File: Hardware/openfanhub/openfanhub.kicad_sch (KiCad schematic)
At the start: 56 parts, among them J1 UART, J2 I2C, J3 Power input, J4 SWD, U1 STM32F103C8T8_Board, U2 AMS1117, U3 USB_HEADER_IN, U4 USB_HEADER_OUT, U5 STM32F103C8Tx, U6 AMS1117, Y1 Crystal

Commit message: Add first (badly) routed version. Still need to polish it and check all power/signal paths
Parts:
- removed J3: Power input, Connector_PinHeader_2.54mm:PinHeader_1x04_P2.54mm_Vertical, symbol Connector:Conn_01x04_Female
- added H1, H2, H3, H4: MountingHole, MountingHole:MountingHole_3.2mm_M3, symbol Mechanical:MountingHole
- added J3: 12V in, Connector_Wire:SolderWire-2.5sqmm_1x01_D2.4mm_OD4.4mm, symbol Connector:Conn_01x01_Male
- added J4: GND in, Connector_Wire:SolderWire-2.5sqmm_1x01_D2.4mm_OD4.4mm, symbol Connector:Conn_01x01_Male
- added J5: 5V IN, Connector_Wire:SolderWire-2.5sqmm_1x01_D2.4mm_OD4.4mm, symbol Connector:Conn_01x01_Male
- renumbered C5 to C1, C13 to C10, C14 to C11, C15 to C12, C16 to C13, C1 to C14, C17 to C15, C2 to C16, C18 to C17, C3 to C18, C4 to C19, C6 to C2, C7 to C3, C8 to C4, C9 to C5, C10 to C6, C11 to C7, C19 to C8, C12 to C9, FB2 to FB1, J4 to J6, R27 to R1, R26 to R10, R2 to R11, R32 to R12, R33 to R13, R3 to R14, R6 to R15, R28 to R2, R4 to R3, R29 to R4, R30 to R5, R5 to R6, R1 to R7, R31 to R8, R25 to R9, U5 to U2, U2 to U3, U6 to U4, U3 to U5, U4 to U6
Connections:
- net +12V: now also J3.1 (Pin_1)
- net +5V: now also J5.1 (Pin_1)
- net FAN1_PWM: now also U1.36 (B8), U2.45 (PB8); no longer U1.26 (A9), U2.30 (PA9)
- net FAN5_PWM: now also U1.26 (A9), U2.30 (PA9); no longer U1.36 (B8), U2.45 (PB8)
- net GND: now also J4.1 (Pin_1)

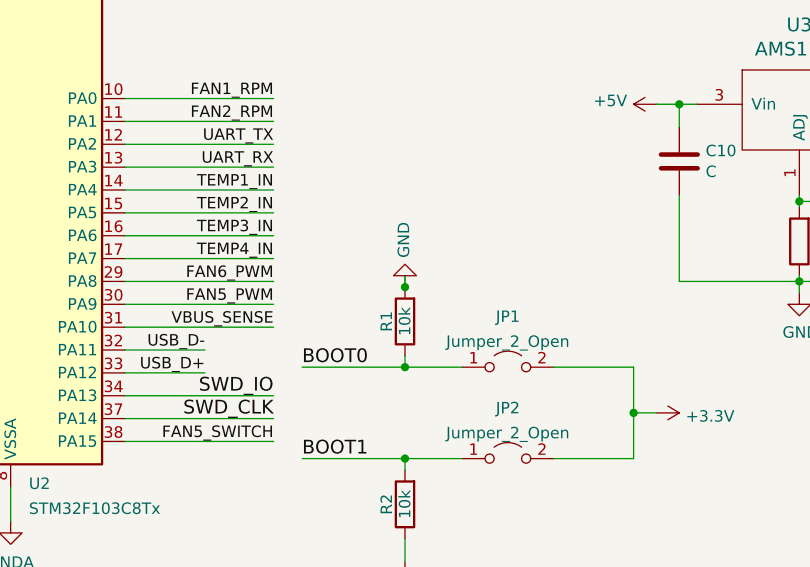
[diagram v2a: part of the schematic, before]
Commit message: Update PCB. Move Power and USB to the same side
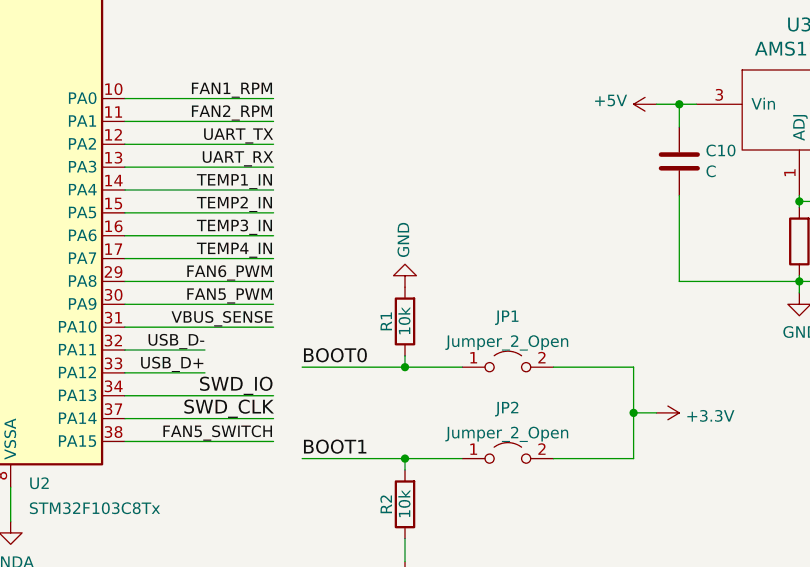
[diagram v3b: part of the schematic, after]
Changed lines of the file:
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@@
   (junction (at 123.19 42.545) (diameter 0) (color 0 0 0 0)
   )
-  (junction (at 116.205 156.21) (diameter 0) (color 0 0 0 0)
-  )
   (junction (at 221.615 136.525) (diameter 0) (color 0 0 0 0)
   )
@@
     (stroke (width 0) (type default) (color 0 0 0 0))
   )
-  (wire (pts (xy 116.205 156.21) (xy 116.205 154.94))
-    (stroke (width 0) (type default) (color 0 0 0 0))
-  )
   (wire (pts (xy 184.785 45.72) (xy 210.185 45.72))
     (stroke (width 0) (type default) (color 0 0 0 0))
@@
     )
     (path "/00000000-0000-0000-0000-000061cbd2d4/400d7499-cda1-432f-a720-e9564b76ff05/00000000-0000-0000-0000-000061cfaf6a"
-      (reference "Q1") (unit 1) (value "Q_NMOS_GSD") (footprint "Package_TO_SOT_SMD:SOT-23")
+      (reference "Q1") (unit 1) (value "IRLML2502") (footprint "Package_TO_SOT_SMD:SOT-23")
     )
     (path "/00000000-0000-0000-0000-000061cbd2d4/400d7499-cda1-432f-a720-e9564b76ff05/832da771-3447-4aa3-a1d5-34305654223f"
-      (reference "Q2") (unit 1) (value "AO449") (footprint "Package_SO:SOIC-8_3.9x4.9mm_P1.27mm")
+      (reference "Q2") (unit 1) (value "AO4409") (footprint "Package_SO:SOIC-8_3.9x4.9mm_P1.27mm")
     )
     (path "/00000000-0000-0000-0000-000061cbd2d4/374ddff5-0da3-4c1a-9cf4-3e7dd0779e2b/00000000-0000-0000-0000-000061cfaf6a"
-      (reference "Q3") (unit 1) (value "Q_NMOS_GSD") (footprint "Package_TO_SOT_SMD:SOT-23")
+      (reference "Q3") (unit 1) (value "IRLML2502") (footprint "Package_TO_SOT_SMD:SOT-23")
     )
     (path "/00000000-0000-0000-0000-000061cbd2d4/374ddff5-0da3-4c1a-9cf4-3e7dd0779e2b/832da771-3447-4aa3-a1d5-34305654223f"
-      (reference "Q4") (unit 1) (value "AO449") (footprint "Package_SO:SOIC-8_3.9x4.9mm_P1.27mm")
+      (reference "Q4") (unit 1) (value "AO4409") (footprint "Package_SO:SOIC-8_3.9x4.9mm_P1.27mm")
     )
     (path "/00000000-0000-0000-0000-000061cbd2d4/00000000-0000-0000-0000-000061cbf096/00000000-0000-0000-0000-000061cfaf6a"
-      (reference "Q5") (unit 1) (value "Q_NMOS_GSD") (footprint "Package_TO_SOT_SMD:SOT-23")
+      (reference "Q5") (unit 1) (value "IRLML2502") (footprint "Package_TO_SOT_SMD:SOT-23")
     )
     (path "/00000000-0000-0000-0000-000061cbd2d4/00000000-0000-0000-0000-000061cbf096/832da771-3447-4aa3-a1d5-34305654223f"
-      (reference "Q6") (unit 1) (value "AO449") (footprint "Package_SO:SOIC-8_3.9x4.9mm_P1.27mm")
+      (reference "Q6") (unit 1) (value "AO4409") (footprint "Package_SO:SOIC-8_3.9x4.9mm_P1.27mm")
     )
     (path "/00000000-0000-0000-0000-000061cbd2d4/00000000-0000-0000-0000-000061caed43/00000000-0000-0000-0000-000061cfaf6a"
-      (reference "Q7") (unit 1) (value "Q_NMOS_GSD") (footprint "Package_TO_SOT_SMD:SOT-23")
+      (reference "Q7") (unit 1) (value "IRLML2502") (footprint "Package_TO_SOT_SMD:SOT-23")
     )
     (path "/00000000-0000-0000-0000-000061cbd2d4/00000000-0000-0000-0000-000061caed43/832da771-3447-4aa3-a1d5-34305654223f"
-      (reference "Q8") (unit 1) (value "AO449") (footprint "Package_SO:SOIC-8_3.9x4.9mm_P1.27mm")
+      (reference "Q8") (unit 1) (value "AO4409") (footprint "Package_SO:SOIC-8_3.9x4.9mm_P1.27mm")
     )
     (path "/00000000-0000-0000-0000-000061cbd2d4/00000000-0000-0000-0000-000061caef29/00000000-0000-0000-0000-000061cfaf6a"
-      (reference "Q9") (unit 1) (value "Q_NMOS_GSD") (footprint "Package_TO_SOT_SMD:SOT-23")
+      (reference "Q9") (unit 1) (value "IRLML2502") (footprint "Package_TO_SOT_SMD:SOT-23")
     )
     (path "/00000000-0000-0000-0000-000061cbd2d4/00000000-0000-0000-0000-000061caef29/832da771-3447-4aa3-a1d5-34305654223f"
-      (reference "Q10") (unit 1) (value "AO449") (footprint "Package_SO:SOIC-8_3.9x4.9mm_P1.27mm")
+      (reference "Q10") (unit 1) (value "AO4409") (footprint "Package_SO:SOIC-8_3.9x4.9mm_P1.27mm")
     )
     (path "/00000000-0000-0000-0000-000061cbd2d4/1d324741-d194-41a3-a0ae-42c211141ec7/00000000-0000-0000-0000-000061cfaf6a"
-      (reference "Q11") (unit 1) (value "Q_NMOS_GSD") (footprint "Package_TO_SOT_SMD:SOT-23")
+      (reference "Q11") (unit 1) (value "IRLML2502") (footprint "Package_TO_SOT_SMD:SOT-23")
     )
     (path "/00000000-0000-0000-0000-000061cbd2d4/1d324741-d194-41a3-a0ae-42c211141ec7/832da771-3447-4aa3-a1d5-34305654223f"
-      (reference "Q12") (unit 1) (value "AO449") (footprint "Package_SO:SOIC-8_3.9x4.9mm_P1.27mm")
+      (reference "Q12") (unit 1) (value "AO4409") (footprint "Package_SO:SOIC-8_3.9x4.9mm_P1.27mm")
     )
     (path "/d1b6e4e2-93c5-474c-8caf-ba7ec8209482"

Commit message: Update (not sure what)
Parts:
- removed D1, D2, D3: D_TVS, Diode_SMD:D_SMB, symbol Device:D_TVS
- added U4: USBLC6-2SC6, Package_TO_SOT_SMD:SOT-23-6, symbol Power_Protection:USBLC6-2SC6
- renumbered R7 to R10, R4 to R3, R5 to R4, R3 to R5, R8 to R6, R6 to R7, R10 to R8, U4 to U5, U5 to U6, U6 to U7
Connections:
- net D1+: now also U4.1 (I/O1); no longer R8.2
- net D1-: now also U4.3 (I/O2); no longer R9.2
- net GND: now also U4.2 (GND)
- net VBUS: now also U4.5 (VBUS)
- new net: R8.2, U4.6 (I/O1)
- new net: R9.2, U4.4 (I/O2)
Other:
- moved on the sheet: R3, R4, R6, R8, R9

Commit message: update
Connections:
- net D1+: now also U6.5 (D1+); no longer U6.4 (D2+)
- net GND: now also U6.8 (GND), U7.8 (GND); no longer U6.2 (GND), U7.2 (GND)
- net VBUS: now also U7.2 (5V); no longer U7.6 (5V)
- net at U7.1 (5V): now also U6.2 (5V); no longer U6.6 (5V)
- net at U7.3 (D1-): now also U6.4 (D2-); no longer U6.8 (D2-)
- net at U6.9 (NO_PIN): no longer U7.4 (D2+)
- net at U7.5 (D1+): now also U6.6 (D2+)
